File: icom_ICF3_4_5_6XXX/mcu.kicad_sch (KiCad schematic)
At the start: 26 parts, among them J1 Conn_01x05, J4 USB_B_Micro, U1 STM32G473CCUx, Y1 8 MHz

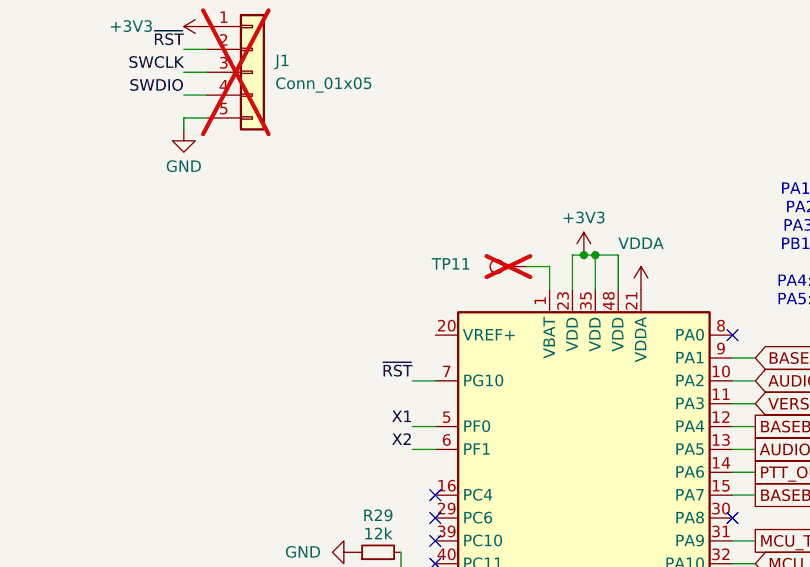
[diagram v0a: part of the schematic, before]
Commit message: ICOM: fixed floating VREF+ pin
KiCAD version bumped up to 9.0.2
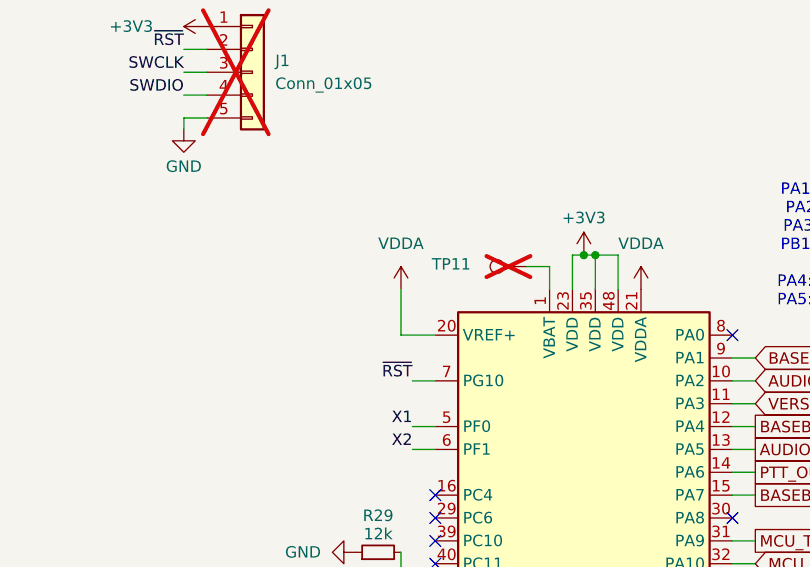
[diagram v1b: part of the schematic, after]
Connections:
- net VDDA: now also U1.20 (VREF+)
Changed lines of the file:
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@@
 (kicad_sch
-	(version 20231120)
+	(version 20250114)
 	(generator "eeschema")
-	(generator_version "8.0")
+	(generator_version "9.0")
 	(paper "A4")
 	(title_block
 		(title "Micro17 - OpenRTX on a Module for ICOM radios")
-		(date "06.03.2024")
+		(date "13.06.2025")
 		(rev "A")
 		(company "Wojciech SP5WWP, Mano ON6RF, Mutlu TA1MD et al.")
 		(comment 1 "M17 Project, OpenRTX")
 	)
+	(text "USART1"
+		(exclude_from_sim no)
+		(at 172.72 90.424 0)
+		(effects
+			(font
+				(size 1.27 1.27)
+			)
+		)
+	)
+	(text "PA1:ADC12_IN2\nPA2:ADC1_IN3\nPA3:ADC1_IN4, \nPB13:ADC3_IN5\n\nPA4:DAC1_OUT1\nPA5:DAC1_OUT2"
+		(exclude_from_sim no)
+		(at 167.132 56.134 0)
+		(effects
+			(font
+				(size 1.27 1.27)
+			)
+		)
+	)
 	(junction
 		(at 207.01 34.29)
@@
 	(wire
 		(pts
+			(xy 118.11 66.04) (xy 121.92 66.04)
+		)
+		(stroke
+			(width 0)
+			(type default)
+		)
+	)
+	(wire
+		(pts
 			(xy 96.52 41.91) (xy 93.98 41.91)
 		)
@@
 	(wire
 		(pts
+			(xy 118.11 60.96) (xy 118.11 66.04)
+		)
+		(stroke
+			(width 0)
+			(type default)
+		)
+	)
+	(wire
+		(pts
 			(xy 119.38 71.12) (xy 121.92 71.12)
 		)
@@
 		)
 	)
-	(text "USART1"
-		(exclude_from_sim no)
-		(at 172.72 90.424 0)
-		(effects
-			(font
-				(size 1.27 1.27)
-			)
-		)
-	)
-	(text "PA1:ADC12_IN2\nPA2:ADC1_IN3\nPA3:ADC1_IN4, \nPB13:ADC3_IN5\n\nPA4:DAC1_OUT1\nPA5:DAC1_OUT2"
-		(exclude_from_sim no)
-		(at 167.132 56.134 0)
-		(effects
-			(font
-				(size 1.27 1.27)
-			)
-		)
-	)
 	(label "~{RST}"
 		(at 119.38 71.12 180)
-		(fields_autoplaced yes)
 		(effects
 			(font
@@
 	(label "SWCLK"
 		(at 170.18 101.6 0)
-		(fields_autoplaced yes)
 		(effects
 			(font
@@
 	(label "X1"
 		(at 52.07 55.88 0)
-		(fields_autoplaced yes)
 		(effects
 			(font
@@
 	(label "SWDIO"
 		(at 93.98 39.37 180)
-		(fields_autoplaced yes)
 		(effects
 			(font
@@
 	(label "SWCLK"
 		(at 93.98 36.83 180)
-		(fields_autoplaced yes)
 		(effects
 			(font
@@
 	(label "X2"
 		(at 66.04 55.88 180)
-		(fields_autoplaced yes)
 		(effects
 			(font
@@
 	(label "BOOT0"
 		(at 114.3 124.46 180)
-		(fields_autoplaced yes)
 		(effects
 			(font
@@
 	(label "SWDIO"
 		(at 170.18 99.06 0)
-		(fields_autoplaced yes)
 		(effects
 			(font
@@
 	(label "X2"
 		(at 119.38 78.74 180)
-		(fields_autoplaced yes)
 		(effects
 			(font
@@
 	(label "X1"
 		(at 119.38 76.2 180)
-		(fields_autoplaced yes)
 		(effects
 			(font
@@
 	(label "~{RST}"
 		(at 93.98 34.29 180)
-		(fields_autoplaced yes)
 		(effects
 			(font
@@
 					(unit 1)
 				)
+			)
+		)
+	)
+	(symbol
+		(lib_id "power:VDDA")
+		(at 118.11 60.96 0)
+		(unit 1)
+		(exclude_from_sim no)
+		(in_bom yes)
+		(on_board yes)
+		(dnp no)
+		(fields_autoplaced yes)
+		(property "Reference" "#PWR083"
+			(at 118.11 64.77 0)
+			(effects
+				(font
+					(size 1.27 1.27)
+				)
+				(hide yes)
+			)
+		)
+		(property "Value" "VDDA"
+			(at 118.11 55.88 0)
+			(effects
+				(font
+					(size 1.27 1.27)
+				)
+			)
+		)
+		(property "Footprint" ""
+			(at 118.11 60.96 0)
+			(effects
+				(font
+					(size 1.27 1.27)
+				)
+				(hide yes)
+			)
+		)
+		(property "Datasheet" ""
+			(at 118.11 60.96 0)
+			(effects
+				(font
+					(size 1.27 1.27)
+				)
+				(hide yes)
+			)
+		)
+		(property "Description" "Power symbol creates a global label with name \"VDDA\""
+			(at 118.11 60.96 0)
+			(effects
+				(font
+					(size 1.27 1.27)
+				)
+				(hide yes)
+			)
+		)
+		(pin "1"
+		)
+		(instances
+			(project "micro17"
+				(path "/8b0d7f56-1962-40c9-8b95-6d4fe558acbc/9f9e0b5b-f07d-4ebd-b315-be375c62719d"
+					(reference "#PWR083")
+					(unit 1)
+				)

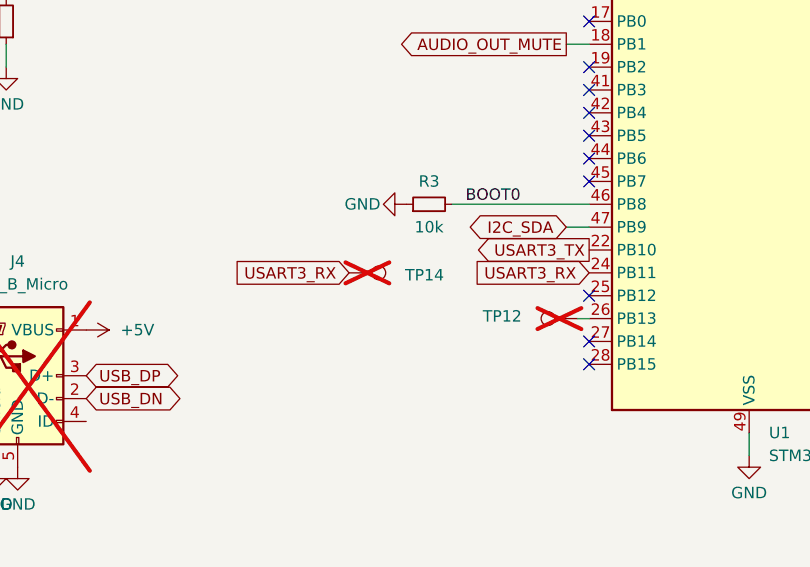
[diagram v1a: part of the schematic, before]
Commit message: re-routed debug UART
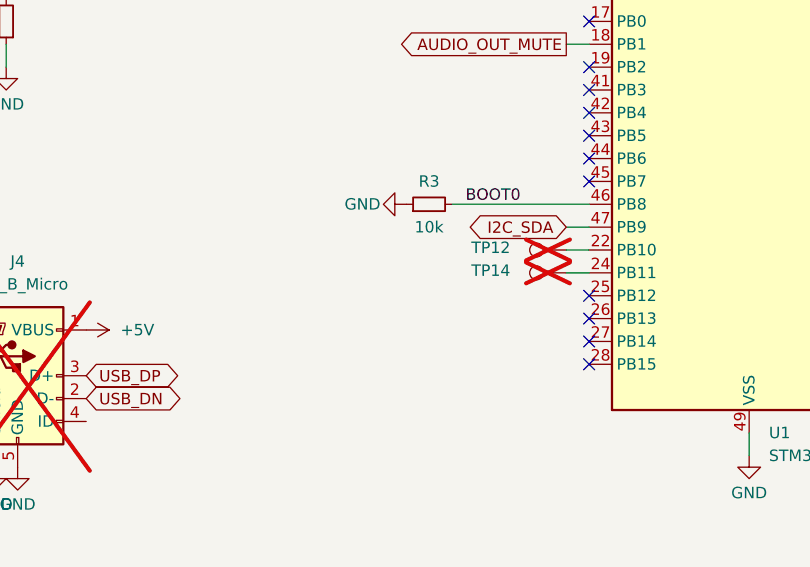
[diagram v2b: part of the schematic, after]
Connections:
- net USART3_TX is gone; now on an unnamed net: U1.22 (PB10)
- net at TP12.1: no longer U1.26 (PB13)
- net USART3_RX: no longer names the net of TP14.1, U1.24 (PB11)
- no-connect marks 18 -> 19
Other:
- moved on the sheet: TP12, TP14
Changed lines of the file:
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@@
+	)
+	(no_connect
+		(at 121.92 137.16)
 	)
 	(no_connect
@@
 	(wire
 		(pts
+			(xy 119.38 132.08) (xy 121.92 132.08)
+		)
+		(stroke
+			(width 0)
+			(type default)
+		)
+	)
+	(wire
+		(pts
 			(xy 207.01 34.29) (xy 207.01 36.83)
 		)
@@
 	(wire
 		(pts
-			(xy 120.65 137.16) (xy 121.92 137.16)
+			(xy 119.38 129.54) (xy 121.92 129.54)
 		)
 		(stroke
@@
 		)
 	)
-	(global_label "USART3_RX"
-		(shape input)
-		(at 121.92 132.08 180)
-		(fields_autoplaced yes)
-		(effects
-			(font
-				(size 1.27 1.27)
-			)
-			(justify right)
-		)
-		(property "Intersheetrefs" "${INTERSHEET_REFS}"
-			(at 108.412 132.08 0)
-			(effects
-				(font
-					(size 1.27 1.27)
-				)
-				(justify right)
-				(hide yes)
-			)
-		)
-	)
-	(global_label "USART3_RX"
-		(shape input)
-		(at 95.25 132.08 180)
-		(fields_autoplaced yes)
-		(effects
-			(font
-				(size 1.27 1.27)
-			)
-			(justify right)
-		)
-		(property "Intersheetrefs" "${INTERSHEET_REFS}"
-			(at 81.742 132.08 0)
-			(effects
-				(font
-					(size 1.27 1.27)
-				)
-				(justify right)
-				(hide yes)
-			)
-		)
-	)
 	(global_label "USB_DN"
 		(shape bidirectional)
@@
 		(property "Intersheetrefs" "${INTERSHEET_REFS}"
 			(at 185.3982 91.44 0)
-			(effects
-				(font
-					(size 1.27 1.27)
-				)
-				(justify right)
-				(hide yes)
-			)
-		)
-	)
-	(global_label "USART3_TX"
-		(shape output)
-		(at 121.92 129.54 180)
-		(fields_autoplaced yes)
-		(effects
-			(font
-				(size 1.27 1.27)
-			)
-			(justify right)
-		)
-		(property "Intersheetrefs" "${INTERSHEET_REFS}"
-			(at 108.7144 129.54 0)
 			(effects
 				(font
@@
 	(symbol
 		(lib_id "Connector:TestPoint")
-		(at 120.65 137.16 90)
+		(at 119.38 129.54 90)
 		(unit 1)
 		(exclude_from_sim no)
@@
 		(dnp yes)
 		(property "Reference" "TP12"
-			(at 112.268 136.906 90)
+			(at 110.998 129.286 90)
 			(effects
 				(font
@@
 		)
 		(property "Value" "GP"
-			(at 115.57 135.8901 90)
+			(at 114.3 128.2701 90)
 			(effects
 				(font
@@
 		)
 		(property "Footprint" "TestPoint:TestPoint_Pad_D1.0mm"
-			(at 120.65 132.08 0)
+			(at 119.38 124.46 0)
 			(effects
 				(font
@@
 		)
 		(property "Datasheet" "~"
-			(at 120.65 132.08 0)
+			(at 119.38 124.46 0)
 			(effects
 				(font
@@
 		)
 		(property "Description" ""
-			(at 120.65 137.16 0)
+			(at 119.38 129.54 0)
 			(effects
 				(font
@@
 		)
 		(property "MPN" ""
-			(at 120.65 137.16 0)
+			(at 119.38 129.54 0)
 			(effects
 				(font
@@
 		)
 		(property "Height" ""
-			(at 120.65 137.16 0)
+			(at 119.38 129.54 0)
 			(effects
 				(font
@@
 		)
 		(property "Manufacturer_Name" ""
-			(at 120.65 137.16 0)
+			(at 119.38 129.54 0)
 			(effects
 				(font
@@
 		)
 		(property "Manufacturer_Part_Number" ""
-			(at 120.65 137.16 0)
+			(at 119.38 129.54 0)
 			(effects
 				(font
@@
 		)
 		(property "Mouser Part Number" ""
-			(at 120.65 137.16 0)
+			(at 119.38 129.54 0)
 			(effects
 				(font
@@
 		)
 		(property "Mouser Price/Stock" ""
-			(at 120.65 137.16 0)
+			(at 119.38 129.54 0)
 			(effects
 				(font
@@
 		)
 		(property "JLC" ""
-			(at 120.65 137.16 0)
+			(at 119.38 129.54 0)
 			(effects
 				(font
@@
 		)
 		(property "PN" ""
-			(at 120.65 137.16 0)
+			(at 119.38 129.54 0)
 			(effects
 				(font
@@
 	(symbol
 		(lib_id "Connector:TestPoint")
-		(at 95.25 132.08 270)
+		(at 119.38 132.08 90)
 		(unit 1)
 		(exclude_from_sim no)
@@
 		(dnp yes)
 		(property "Reference" "TP14"
-			(at 103.632 132.334 90)
+			(at 110.998 131.826 90)
 			(effects
 				(font
@@
 		)
 		(property "Value" "GP"
-			(at 100.33 133.3499 90)
+			(at 114.3 130.8101 90)
 			(effects
 				(font
@@
 		)
 		(property "Footprint" "TestPoint:TestPoint_Pad_D1.0mm"
-			(at 95.25 137.16 0)
+			(at 119.38 127 0)
 			(effects
 				(font
@@
 		)
 		(property "Datasheet" "~"
-			(at 95.25 137.16 0)
+			(at 119.38 127 0)
 			(effects
 				(font
@@
 		)
 		(property "Description" ""
-			(at 95.25 132.08 0)
+			(at 119.38 132.08 0)
 			(effects
 				(font
@@
 		)
 		(property "MPN" ""
-			(at 95.25 132.08 0)
+			(at 119.38 132.08 0)
 			(effects
 				(font
@@
 		)
 		(property "Height" ""
-			(at 95.25 132.08 0)
+			(at 119.38 132.08 0)
 			(effects
 				(font
@@
 		)
 		(property "Manufacturer_Name" ""
-			(at 95.25 132.08 0)
+			(at 119.38 132.08 0)
 			(effects
 				(font
@@
 		)
 		(property "Manufacturer_Part_Number" ""
-			(at 95.25 132.08 0)
+			(at 119.38 132.08 0)
 			(effects
 				(font
@@
 		)
 		(property "Mouser Part Number" ""
-			(at 95.25 132.08 0)
+			(at 119.38 132.08 0)
 			(effects
 				(font
@@
 		)
 		(property "Mouser Price/Stock" ""
-			(at 95.25 132.08 0)
+			(at 119.38 132.08 0)
 			(effects
 				(font
@@
 		)
 		(property "JLC" ""
-			(at 95.25 132.08 0)
+			(at 119.38 132.08 0)
 			(effects
 				(font
@@
 		)
 		(property "PN" ""
-			(at 95.25 132.08 0)
-			(effects
-				(font
+			(at 119.38 132.08 0)
+			(effects
+				(font
